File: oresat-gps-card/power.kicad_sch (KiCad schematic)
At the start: 94 parts, among them Q1 DMP2240UDM, Q2 PMV45EN, Q3 DMP3050LVT-7, Q4 DMP3050LVT-7, Q5 PMV45EN, U2 MAX7310ATE, U3 MIC842LYC5, U4 MIC842LYC5, U5 MAX4211FETE, U6 LTC3624, U7 TS5A21366

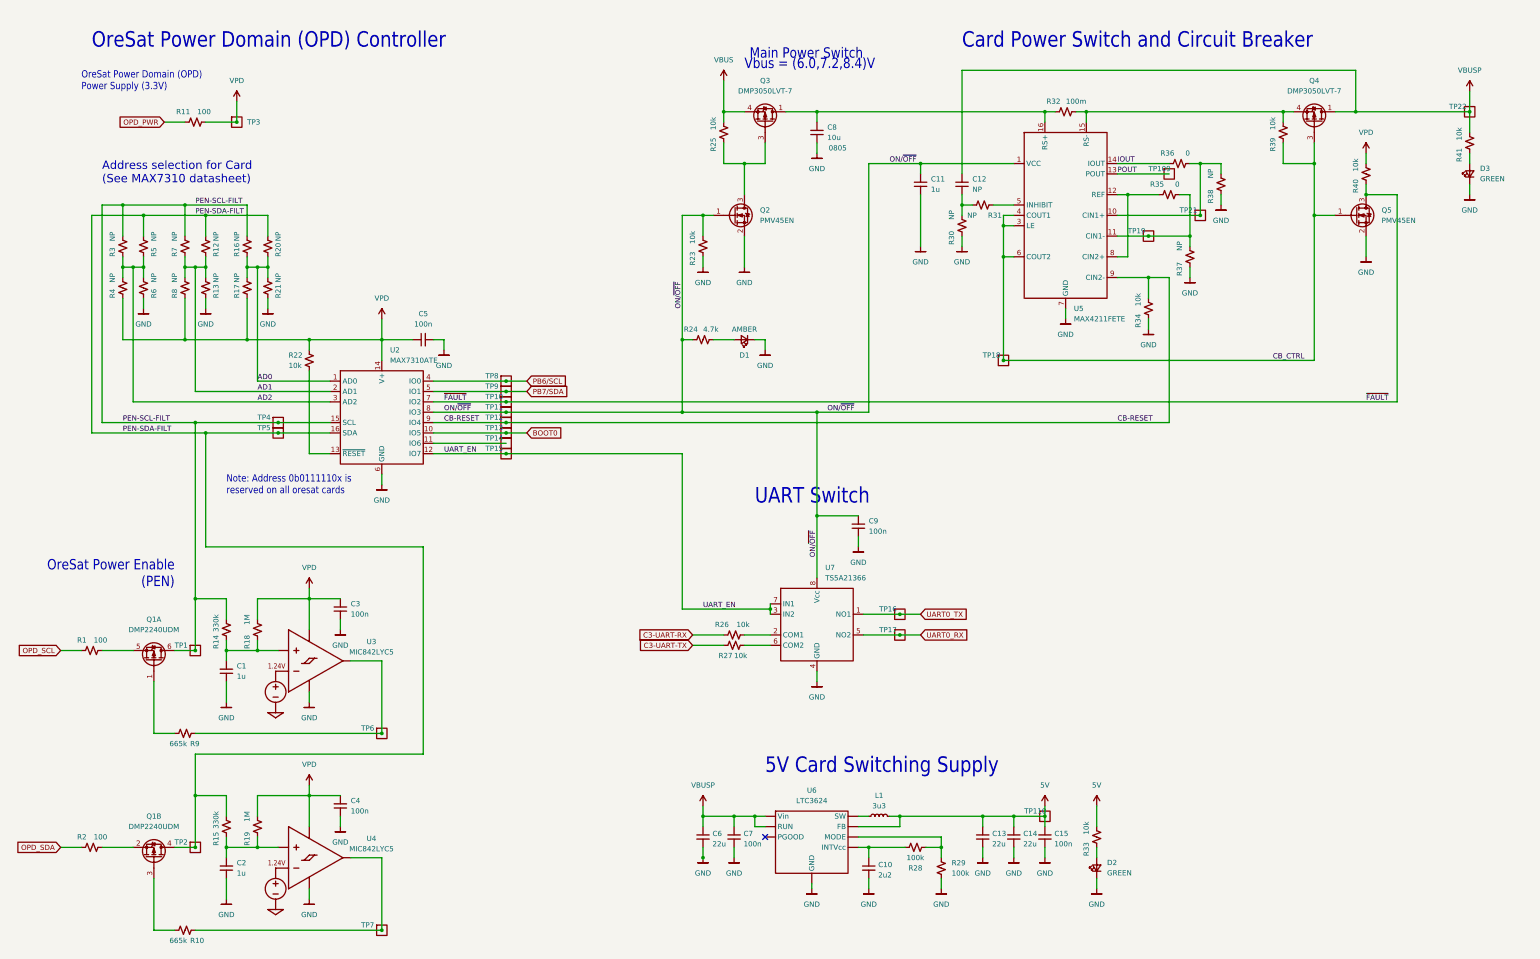
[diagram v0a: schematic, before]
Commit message: GPS card design review changes and issue fixes
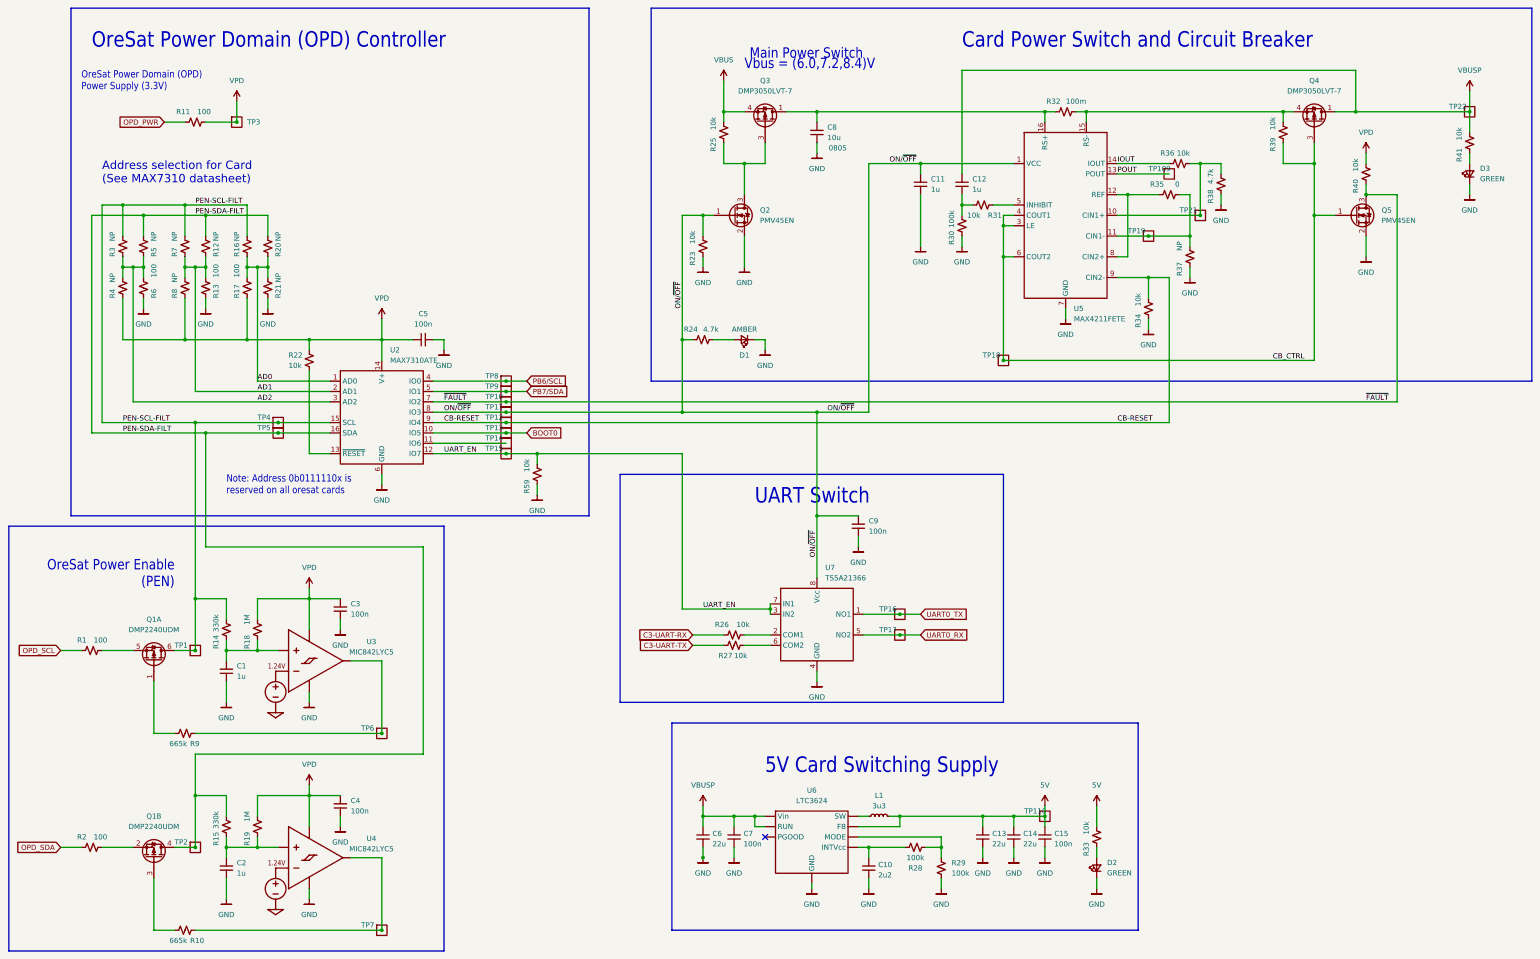
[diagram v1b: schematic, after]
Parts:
- added R59: 10k, Resistor_SMD:R_0603_1608Metric, symbol Device:R_Small_US
- C12: value NP -> 1u
- R13, R17, R6: value NP -> 100
- R30: value NP -> 100k
- R31: value NP -> 10k
- R36: value 0 -> 10k
- R38: value NP -> 4.7k
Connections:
- net GND: now also R59.1
- net UART_EN: now also R59.2
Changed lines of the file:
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@@
   (junction (at 251.46 66.04) (diameter 0) (color 0 0 0 0)
   )
+  (junction (at 147.32 127) (diameter 0) (color 0 0 0 0)
+  )
   (junction (at 73.66 45.72) (diameter 0) (color 0 0 0 0)
   )
@@
     (stroke (width 0) (type default) (color 0 0 0 0))
   )
+  (wire (pts (xy 147.32 127) (xy 182.88 127))
+    (stroke (width 0) (type default) (color 0 0 0 0))
+  )
   (wire (pts (xy 215.9 142.24) (xy 226.06 142.24))
     (stroke (width 0) (type default) (color 0 0 0 0))
@@
     (stroke (width 0) (type default) (color 0 0 0 0))
   )
+  (polyline (pts (xy 180.34 193.04) (xy 180.34 243.84))
+    (stroke (width 0) (type default) (color 0 0 0 0))
+  )
   (wire (pts (xy 182.88 127) (xy 182.88 165.1))
     (stroke (width 0) (type default) (color 0 0 0 0))
@@
     (stroke (width 0) (type default) (color 0 0 0 0))
   )
+  (polyline (pts (xy 180.34 193.04) (xy 294.64 193.04))
+    (stroke (width 0) (type default) (color 0 0 0 0))
+  )
   (wire (pts (xy 38.1 121.92) (xy 66.04 121.92))
     (stroke (width 0) (type default) (color 0 0 0 0))
@@
     (stroke (width 0) (type default) (color 0 0 0 0))
   )
+  (polyline (pts (xy 160.02 17.78) (xy 33.02 17.78))
+    (stroke (width 0) (type default) (color 0 0 0 0))
+  )
+  (polyline (pts (xy 261.62 187.96) (xy 261.62 132.08))
+    (stroke (width 0) (type default) (color 0 0 0 0))
+  )
   (wire (pts (xy 71.12 167.64) (xy 71.12 162.56))
     (stroke (width 0) (type default) (color 0 0 0 0))
@@
     (stroke (width 0) (type default) (color 0 0 0 0))
   )
+  (polyline (pts (xy 17.78 144.78) (xy 124.46 144.78))
+    (stroke (width 0) (type default) (color 0 0 0 0))
+  )
   (wire (pts (xy 347.98 33.02) (xy 347.98 43.18))
     (stroke (width 0) (type default) (color 0 0 0 0))
@@
     (stroke (width 0) (type default) (color 0 0 0 0))
   )
+  (polyline (pts (xy 124.46 248.92) (xy 124.46 144.78))
+    (stroke (width 0) (type default) (color 0 0 0 0))
+  )
   (wire (pts (xy 193.04 45.72) (xy 193.04 43.18))
     (stroke (width 0) (type default) (color 0 0 0 0))
@@
     (stroke (width 0) (type default) (color 0 0 0 0))
   )
+  (polyline (pts (xy 180.34 243.84) (xy 294.64 243.84))
+    (stroke (width 0) (type default) (color 0 0 0 0))
+  )
   (wire (pts (xy 187.96 215.9) (xy 187.96 218.44))
     (stroke (width 0) (type default) (color 0 0 0 0))
   )
+  (polyline (pts (xy 160.02 142.24) (xy 160.02 17.78))
+    (stroke (width 0) (type default) (color 0 0 0 0))
+  )
   (wire (pts (xy 187.96 213.36) (xy 187.96 215.9))
     (stroke (width 0) (type default) (color 0 0 0 0))
@@
     (stroke (width 0) (type default) (color 0 0 0 0))
   )
+  (wire (pts (xy 147.32 134.62) (xy 147.32 137.16))
+    (stroke (width 0) (type default) (color 0 0 0 0))
+  )
   (wire (pts (xy 121.92 109.22) (xy 139.7 109.22))
     (stroke (width 0) (type default) (color 0 0 0 0))
@@
     (stroke (width 0) (type default) (color 0 0 0 0))
   )
+  (polyline (pts (xy 167.64 132.08) (xy 261.62 132.08))
+    (stroke (width 0) (type default) (color 0 0 0 0))
+  )
   (wire (pts (xy 78.74 215.9) (xy 78.74 210.82))
     (stroke (width 0) (type default) (color 0 0 0 0))
@@
     (stroke (width 0) (type default) (color 0 0 0 0))
   )
+  (polyline (pts (xy 391.16 109.22) (xy 175.26 109.22))
+    (stroke (width 0) (type default) (color 0 0 0 0))
+  )
   (wire (pts (xy 182.88 116.84) (xy 182.88 99.06))
     (stroke (width 0) (type default) (color 0 0 0 0))
@@
     (stroke (width 0) (type default) (color 0 0 0 0))
   )
+  (polyline (pts (xy 17.78 144.78) (xy 17.78 248.92))
+    (stroke (width 0) (type default) (color 0 0 0 0))
+  )
   (wire (pts (xy 109.22 93.98) (xy 109.22 99.06))
     (stroke (width 0) (type default) (color 0 0 0 0))
@@
     (stroke (width 0) (type default) (color 0 0 0 0))
   )
-  (wire (pts (xy 139.7 127) (xy 182.88 127))
+  (wire (pts (xy 139.7 127) (xy 147.32 127))
     (stroke (width 0) (type default) (color 0 0 0 0))
   )
@@
     (stroke (width 0) (type default) (color 0 0 0 0))
   )
+  (polyline (pts (xy 33.02 142.24) (xy 160.02 142.24))
+    (stroke (width 0) (type default) (color 0 0 0 0))
+  )
   (wire (pts (xy 45.72 88.9) (xy 45.72 99.06))
     (stroke (width 0) (type default) (color 0 0 0 0))
@@
     (stroke (width 0) (type default) (color 0 0 0 0))
   )
+  (polyline (pts (xy 167.64 187.96) (xy 261.62 187.96))
+    (stroke (width 0) (type default) (color 0 0 0 0))
+  )
   (wire (pts (xy 228.6 223.52) (xy 226.06 223.52))
     (stroke (width 0) (type default) (color 0 0 0 0))
@@
     (stroke (width 0) (type default) (color 0 0 0 0))
   )
+  (polyline (pts (xy 175.26 109.22) (xy 175.26 17.78))
+    (stroke (width 0) (type default) (color 0 0 0 0))
+  )
+  (wire (pts (xy 147.32 127) (xy 147.32 129.54))
+    (stroke (width 0) (type default) (color 0 0 0 0))
+  )
   (wire (pts (xy 292.1 63.5) (xy 289.56 63.5))
     (stroke (width 0) (type default) (color 0 0 0 0))
@@
     (stroke (width 0) (type default) (color 0 0 0 0))
   )
+  (polyline (pts (xy 33.02 17.78) (xy 33.02 142.24))
+    (stroke (width 0) (type default) (color 0 0 0 0))
+  )
   (wire (pts (xy 76.2 73.66) (xy 76.2 66.04))
     (stroke (width 0) (type default) (color 0 0 0 0))
@@
     (stroke (width 0) (type default) (color 0 0 0 0))
   )
+  (polyline (pts (xy 175.26 17.78) (xy 391.16 17.78))
+    (stroke (width 0) (type default) (color 0 0 0 0))
+  )
   (wire (pts (xy 91.44 127) (xy 91.44 106.68))
     (stroke (width 0) (type default) (color 0 0 0 0))
@@
     (stroke (width 0) (type default) (color 0 0 0 0))
   )
+  (polyline (pts (xy 17.78 248.92) (xy 124.46 248.92))
+    (stroke (width 0) (type default) (color 0 0 0 0))
+  )
   (wire (pts (xy 71.12 231.14) (xy 71.12 236.22))
     (stroke (width 0) (type default) (color 0 0 0 0))
@@
     (stroke (width 0) (type default) (color 0 0 0 0))
   )
+  (polyline (pts (xy 391.16 17.78) (xy 391.16 109.22))
+    (stroke (width 0) (type default) (color 0 0 0 0))
+  )
   (wire (pts (xy 121.92 116.84) (xy 139.7 116.84))
     (stroke (width 0) (type default) (color 0 0 0 0))
@@
     (stroke (width 0) (type default) (color 0 0 0 0))
   )
+  (polyline (pts (xy 167.64 132.08) (xy 167.64 187.96))
+    (stroke (width 0) (type default) (color 0 0 0 0))
+  )
   (wire (pts (xy 251.46 63.5) (xy 251.46 66.04))
     (stroke (width 0) (type default) (color 0 0 0 0))
@@
     (stroke (width 0) (type default) (color 0 0 0 0))
   )
+  (polyline (pts (xy 294.64 243.84) (xy 294.64 193.04))
+    (stroke (width 0) (type default) (color 0 0 0 0))
+  )
   (wire (pts (xy 81.28 81.28) (xy 81.28 83.82))
     (stroke (width 0) (type default) (color 0 0 0 0))
@@
       (effects (font (size 1.27 1.27)) (justify left))
     )
-    (property "Value" "NP" (id 1) (at 312.42 57.15 90)
+    (property "Value" "4.7k" (id 1) (at 312.42 57.15 90)
       (effects (font (size 1.27 1.27)) (justify left))
     )
@@
     (pin "1")
   )
+  (symbol (lib_id "Device:R_Small_US") (at 147.32 132.08 180) (unit 1)
+    (in_bom yes) (on_board yes)
+    (property "Reference" "R59" (id 0) (at 144.78 133.35 90)
+      (effects (font (size 1.27 1.27)) (justify left))
+    )
+    (property "Value" "10k" (id 1) (at 144.78 128.27 90)
+      (effects (font (size 1.27 1.27)) (justify left))
+    )
+    (property "Footprint" "Resistor_SMD:R_0603_1608Metric" (id 2) (at 147.32 132.08 0)
+      (effects (font (size 1.27 1.27)) hide)
+    )
+    (property "Datasheet" "~" (id 3) (at 147.32 132.08 0)
+      (effects (font (size 1.27 1.27)) hide)
+    )
+    (pin "1")
+    (pin "2")
+  )
   (symbol (lib_id "Device:R_Small_US") (at 66.04 86.36 0) (unit 1)
     (in_bom yes) (on_board yes)
@@
       (effects (font (size 1.27 1.27)) (justify left))
     )
-    (property "Value" "NP" (id 1) (at 68.58 85.09 90)
+    (property "Value" "100" (id 1) (at 68.58 83.82 90)
       (effects (font (size 1.27 1.27)) (justify left))
     )
@@
       (effects (font (size 1.27 1.27)) (justify left))
     )
-    (property "Value" "NP" (id 1) (at 53.34 85.09 90)
+    (property "Value" "100" (id 1) (at 53.34 83.82 90)
       (effects (font (size 1.27 1.27)) (justify left))
     )
@@
       (effects (font (size 1.27 1.27)) (justify right))
     )
-    (property "Value" "NP" (id 1) (at 254 62.2235 0)
+    (property "Value" "1u" (id 1) (at 254 62.2235 0)
       (effects (font (size 1.27 1.27)) (justify right))
     )
@@
     (pin "1")
   )
+  (symbol (lib_id "OreSat-Power:GND") (at 147.32 137.16 0) (unit 1)
+    (in_bom yes) (on_board yes) (fields_autoplaced)
+    (property "Reference" "#GND0183" (id 0) (at 147.32 143.51 0)
+      (effects (font (size 1.27 1.27)) hide)
+    )
+    (property "Value" "GND" (id 1) (at 147.32 140.97 0))
+    (property "Footprint" "" (id 2) (at 147.32 137.16 0)
+      (effects (font (size 1.27 1.27)) hide)
+    )
+    (property "Datasheet" "" (id 3) (at 147.32 137.16 0)
+      (effects (font (size 1.27 1.27)) hide)
+    )
+    (pin "1")
+  )
   (symbol (lib_id "Q-DiodesInc-DMP3050LVT-PCH-Mosfet:DMP3050LVT-7") (at 337.82 45.72 270) (mirror x) (unit 1)
     (in_bom yes) (on_board yes) (fields_autoplaced)
@@
       (effects (font (size 1.27 1.27)) (justify left))
     )
-    (property "Value" "NP" (id 1) (at 73.66 85.09 90)
+    (property "Value" "100" (id 1) (at 73.66 83.82 90)
       (effects (font (size 1.27 1.27)) (justify left))
     )
@@
       (effects (font (size 1.27 1.27)) (justify left))
     )
-    (property "Value" "NP" (id 1) (at 248.92 67.31 90)
+    (property "Value" "100k" (id 1) (at 248.92 67.31 90)
       (effects (font (size 1.27 1.27)) (justify left))
     )
@@
       (effects (font (size 1.27 1.27)) (justify left))
     )
-    (property "Value" "NP" (id 1) (at 252.73 68.58 90)
+    (property "Value" "10k" (id 1) (at 252.73 68.58 90)
       (effects (font (size 1.27 1.27)) (justify left))
     )
@@
       (effects (font (size 1.27 1.27)) (justify left))
     )
-    (property "Value" "0" (id 1) (at 307.34 53.34 90)
+    (property "Value" "10k" (id 1) (at 307.34 53.34 90)
       (effects (font (size 1.27 1.27)) (justify left))
     )
